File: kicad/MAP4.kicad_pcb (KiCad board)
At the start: 2 copper layers, 9 parts, among them P2 Pin

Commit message: work in progress
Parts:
- moved P2 239.3 mm to (-0.10, -24.1)
- moved D1 239.0 mm to (0.00, -17.0)
- moved R1 238.9 mm to (0.00, -12.2)
- moved D3 238.3 mm to (-17.2, 10.0), turned to 30 degrees
- moved R2 237.9 mm to (12.5, 7.50), turned to 60 degrees
- moved G*** 237.9 mm to (-0.10, -2.40)
- moved R3 237.0 mm to (-12.5, 7.50), turned to 120 degrees
- moved D2 236.9 mm to (17.2, 10.0), turned to 150 degrees
- moved BT1 236.5 mm to (0.00, 1.00)
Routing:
- net /3V: track 0.00 -> 81.1 mm
- net /GND: track 0.00 -> 64.0 mm
- net /LED_grn: track 0.00 -> 9.40 mm
- net /LED_blu: track 0.00 -> 9.40 mm
- net /LED_red: track 0.00 -> 6.99 mm
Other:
- board outline added: 49.8 x 48.9 mm

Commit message: MAP4 complete. Boards ordered out
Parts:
- removed G***: LOGO, map4_fp:MA_LOGO4
- added LOGO1: OPEN_HARDWARE_1, map4_fp:Logo_silk_OSHW_6x6mm, B.Cu at (135.0, 112.2)
- added P1: Logo_MA, map4_fp:MA_LOGO4, F.Cu at (149.9, 97.5)
- added P3: Pin, map4_fp:MTG_0mm8, F.Cu at (145.8, 80.0)
- added P4: Pin, map4_fp:MTG_0mm8, F.Cu at (145.8, 78.0)
- added P5: Pin, map4_fp:MTG_0mm8, F.Cu at (154.2, 80.0)
- added P6: Pin, map4_fp:MTG_0mm8, F.Cu at (154.2, 78.0)
- D1: value LED Red -> Red
- D2: value LED Grn -> Grn
- D3: value LED Blu -> Blu
- moved R2 181.1 mm to (163.5, 107.5)
- moved P2 180.4 mm to (150.0, 75.8)
- moved D1 180.3 mm to (150.0, 83.0)
- moved D2 180.3 mm to (167.2, 110.0)
- moved D3 180.3 mm to (132.8, 110.0)
- moved R1 180.3 mm to (150.0, 87.8)
- moved BT1 179.7 mm to (150.0, 100.0)
- moved R3 179.4 mm to (136.5, 107.5)
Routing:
- net /3V: track 81.1 -> 126.4 mm
- net /GND: track 64.0 -> 98.9 mm
- net /LED_grn: track 9.40 -> 7.84 mm
- net /LED_blu: track 9.40 -> 7.84 mm
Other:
- board text added: "EASY"
- board text added: "HERE'S MY MAP4 SKILL BADGE"
- board text added: "IS"
- board text added: "MAKER'S ASYLUM"
- board text added: "SOLDERING"
- board text added: "[+]"
- board text added: "[-]"

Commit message: MAP4 revised Gerbers to clear PCBpower issue
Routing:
- net /LED_red: track 6.99 -> 13.2 mm
- net /LED_grn: track 7.84 -> 13.5 mm
- net /LED_blu: track 7.84 -> 13.5 mm
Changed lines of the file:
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@@
     (links 17)
     (no_connects 0)
-    (area 124.974637 71.588459 174.973189 120.625001)
+    (area 111.500001 71.5 175.000001 126.7)
     (thickness 1.6)
     (drawings 21)
-    (tracks 51)
+    (tracks 63)
     (zones 0)
     (modules 14)
@@
   )
   (layers
-    (0 F.Cu signal hide)
+    (0 F.Cu signal)
     (31 B.Cu signal)
     (32 B.Adhes user)
@@
       (outputformat 4)
       (mirror false)
-      (drillshape 0)
+      (drillshape 2)
       (scaleselection 1)
       (outputdirectory pdf/))
@@
   (gr_arc (start 150 100) (end 163.2 115.75) (angle 79.93242788) (layer Edge.Cuts) (width 0.15))
   (gr_line (start 171.5 115.75) (end 163.2 115.75) (layer Edge.Cuts) (width 0.15))
+  (segment (start 158.1 100) (end 163 100) (width 1) (layer B.Cu) (net 1) (status C00000))
+  (segment (start 150 81.73) (end 148.77 81.73) (width 1) (layer F.Cu) (net 1) (status 400000))
+  (segment (start 144.10099 83.5) (end 144.10099 83.499999) (width 1) (layer F.Cu) (net 1))
+  (segment (start 147 83.5) (end 144.10099 83.5) (width 1) (layer F.Cu) (net 1))
+  (segment (start 148.77 81.73) (end 147 83.5) (width 1) (layer F.Cu) (net 1))
+  (segment (start 150 81.73) (end 151.73 81.73) (width 1) (layer F.Cu) (net 1) (status 400000))
+  (segment (start 153.5 83.5) (end 155.37 83.5) (width 1) (layer F.Cu) (net 1))
+  (segment (start 151.73 81.73) (end 153.5 83.5) (width 1) (layer F.Cu) (net 1))
   (segment (start 163 100) (end 165.93 100) (width 1) (layer F.Cu) (net 1))
-  (segment (start 158.1 100) (end 163 100) (width 1) (layer F.Cu) (net 1))
-  (segment (start 150 81.73) (end 154.25 81.75) (width 1) (layer F.Cu) (net 1))
-  (segment (start 154.25 81.75) (end 165.93 100) (width 1) (layer F.Cu) (net 1))
+  (segment (start 155.37 83.5) (end 165.93 100) (width 1) (layer F.Cu) (net 1))
   (segment (start 165.93 100) (end 166.57 101) (width 1) (layer F.Cu) (net 1))
   (segment (start 166.57 101) (end 170.25 106.75) (width 1) (layer F.Cu) (net 1))
   (segment (start 170.25 106.75) (end 168.349852 110.635) (width 1) (layer F.Cu) (net 1))
-  (segment (start 145.27 81.73) (end 129.005001 106.356852) (width 1) (layer F.Cu) (net 1))
-  (segment (start 150 81.73) (end 145.27 81.73) (width 1) (layer F.Cu) (net 1))
+  (segment (start 144.10099 83.499999) (end 129.005001 106.356852) (width 1) (layer F.Cu) (net 1))
   (segment (start 129.005001 106.356852) (end 131.650148 110.635) (width 1) (layer F.Cu) (net 1))
   (segment (start 168.349852 110.635) (end 166.25 114.5) (width 1) (layer F.Cu) (net 1) (status 10))
   (segment (start 166.25 114.5) (end 134.25 114.5) (width 1) (layer F.Cu) (net 1))
   (segment (start 134.25 114.5) (end 131.650148 110.635) (width 1) (layer F.Cu) (net 1) (status 20))
+  (segment (start 136 100) (end 138.2 100) (width 1) (layer B.Cu) (net 2) (status C00000))
   (segment (start 138.532 111.019527) (end 144.230473 111.019527) (width 1) (layer F.Cu) (net 2))
   (segment (start 138.532 111.019527) (end 138.532 109.879724) (width 1) (layer F.Cu) (net 2))
@@
   (segment (start 155.25 110.5) (end 155.25 98) (width 1) (layer F.Cu) (net 2))
   (segment (start 144.75 97.5) (end 144.5 97.5) (width 1) (layer F.Cu) (net 2))
+  (segment (start 144.5 97.5) (end 141.5 94.5) (width 1) (layer F.Cu) (net 2))
+  (segment (start 141.5 94.5) (end 140.5 94.5) (width 1) (layer F.Cu) (net 2))
+  (segment (start 140.5 94.5) (end 138.2 96.8) (width 1) (layer F.Cu) (net 2))
   (segment (start 138.2 96.8) (end 138.2 100) (width 1) (layer F.Cu) (net 2))
-  (segment (start 140.5 94.5) (end 138.2 96.8) (width 1) (layer F.Cu) (net 2))
-  (segment (start 141.5 94.5) (end 140.5 94.5) (width 1) (layer F.Cu) (net 2))
-  (segment (start 144.5 97.5) (end 141.5 94.5) (width 1) (layer F.Cu) (net 2))
-  (segment (start 136 100) (end 138.2 100) (width 1) (layer F.Cu) (net 2))
   (segment (start 144.75 97.5) (end 145.5 97.5) (width 1) (layer F.Cu) (net 2))
   (segment (start 145.5 97.5) (end 150.25 102.25) (width 1) (layer F.Cu) (net 2))
@@
   (segment (start 158 95.25) (end 155.25 98) (width 1) (layer F.Cu) (net 2))
   (segment (start 145.936 87.75) (end 149.05 87.75) (width 1) (layer F.Cu) (net 2) (status 30))
+  (segment (start 150 84.27) (end 151.77 84.27) (width 1) (layer B.Cu) (net 3) (status 400000))
+  (segment (start 154.064 86.564) (end 154.064 87.75) (width 1) (layer B.Cu) (net 3) (status 800000))
+  (segment (start 151.77 84.27) (end 154.064 86.564) (width 1) (layer B.Cu) (net 3))
   (segment (start 150.95 87.75) (end 150.95 85.22) (width 1) (layer F.Cu) (net 3) (status 10))
   (segment (start 150.95 85.22) (end 150 84.27) (width 1) (layer F.Cu) (net 3) (status 20))
   (segment (start 154.064 87.75) (end 150.95 87.75) (width 1) (layer F.Cu) (net 3) (status 30))
+  (segment (start 166.150148 109.365) (end 166.150148 104.598621) (width 1) (layer B.Cu) (net 4) (status 400000))
+  (segment (start 166.150148 104.598621) (end 165.532 103.980473) (width 1) (layer B.Cu) (net 4) (status 800000))
   (segment (start 166.150148 109.365) (end 166.150148 105.738424) (width 1) (layer F.Cu) (net 4))
   (segment (start 166.150148 105.738424) (end 165.532 105.120276) (width 1) (layer F.Cu) (net 4))
   (segment (start 165.532 103.980473) (end 165.532 105.120276) (width 1) (layer F.Cu) (net 4))
   (segment (start 165.532 105.120276) (end 163.975 106.677276) (width 1) (layer F.Cu) (net 4))
+  (segment (start 133.849852 109.365) (end 133.849852 104.598621) (width 1) (layer B.Cu) (net 5) (status 400000))
+  (segment (start 133.849852 104.598621) (end 134.468 103.980473) (width 1) (layer B.Cu) (net 5) (status 800000))
   (segment (start 134.468 105.120276) (end 136.025 106.677276) (width 1) (layer F.Cu) (net 5))
   (segment (start 133.849852 109.365) (end 133.849852 105.738424) (width 1) (layer F.Cu) (net 5))

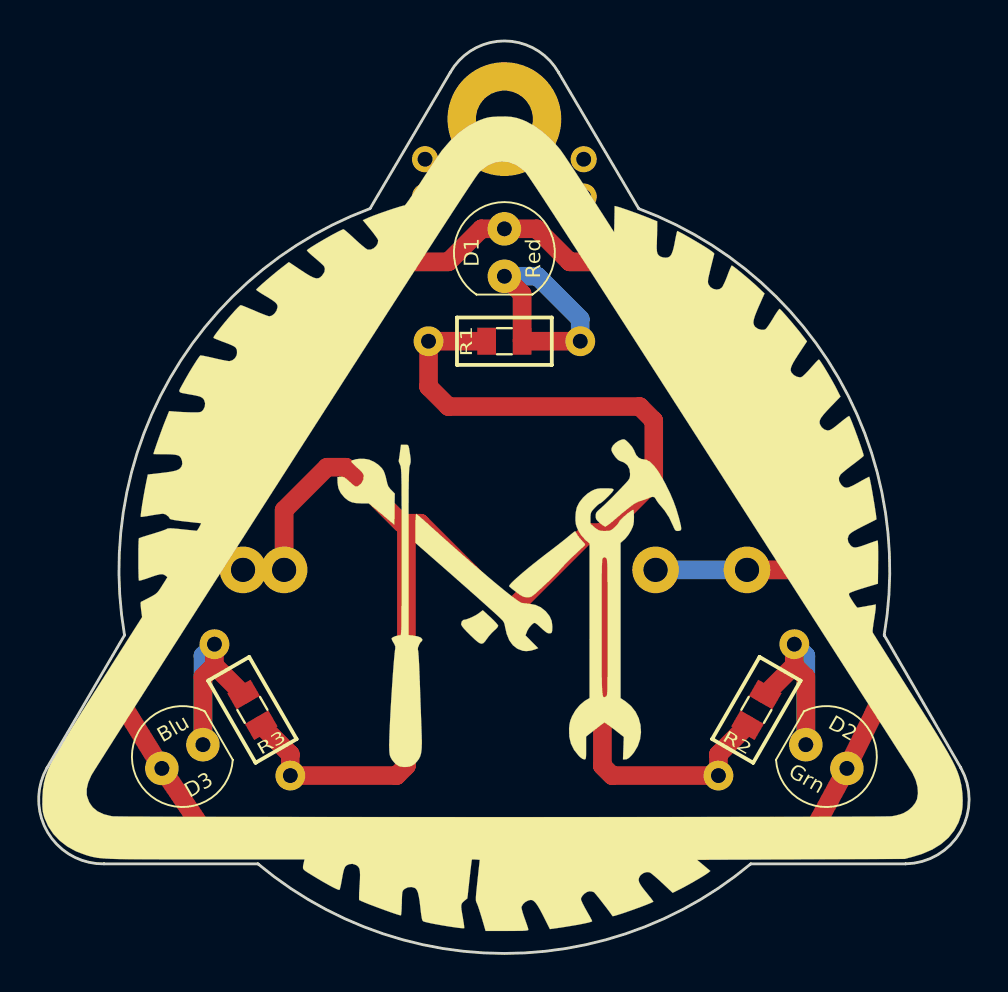
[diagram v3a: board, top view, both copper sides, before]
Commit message: Battery holder footprint correction. New Legend
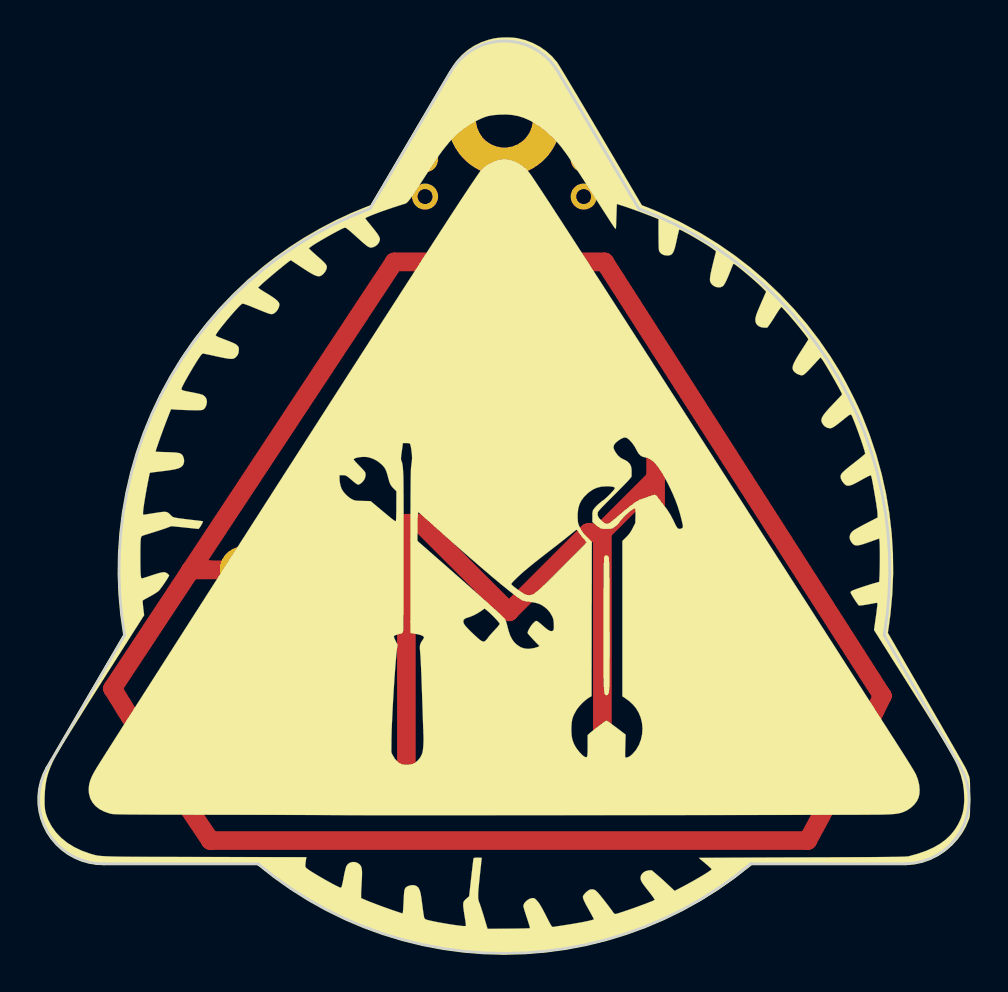
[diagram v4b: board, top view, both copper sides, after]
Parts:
- BT1: footprint map4_fp:cr2032_01 -> map4_fp:cr2032_02
- P1: footprint map4_fp:MA_LOGO4 -> map4_fp:MA_LOGO8
- R1, R2, R3: moved to B.Cu
- moved LOGO1 15.7 mm to (150.0, 107.5)
- moved P1 1.50 mm to (150.0, 96.0)
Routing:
- net /GND: track 98.9 -> 94.7 mm
- net /3V: track 126.0 -> 123.1 mm
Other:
- board text added: "I CAN SOLDER !"
- board text added: "MAP4 https://git.io/von5w"
- board text added: "SPACE FOR ETOK MARK AND CODE"
- board text added: "if it smells like chicken you're holding it wrong !"
- board text added: "makersasylum.com"
- board text removed: "EASY"
- board text removed: "HERE'S MY MAP4 SKILL BADGE"
- board text removed: "IS"
- board text removed: "MAKER'S ASYLUM"
- board text removed: "SOLDERING"
